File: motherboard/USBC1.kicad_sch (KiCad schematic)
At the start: 24 parts, among them J1 USB_C_Receptacle, U10 TPD4E02B04, U29 TVS2200DRV, U6 SY6280AAC, U7 FUSB302BMPX, U8 TPD4E02B04, U9 TPD4E02B04

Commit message: v0.2 75 routes left!
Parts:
- added R55: 10k, Resistor_SMD:R_0402_1005Metric, symbol Device:R_Small
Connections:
- net +3.3V: now also R55.1
- net FUSB_INT: now also R55.2
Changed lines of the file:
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@@
 	)
 	(junction
+		(at 100.33 109.22)
+		(diameter 0)
+		(color 0 0 0 0)
+	)
+	(junction
 		(at 156.21 77.47)
 		(diameter 0)
@@
 	)
 	(junction
+		(at 80.01 125.73)
+		(diameter 0)
+		(color 0 0 0 0)
+	)
+	(junction
 		(at 176.53 86.36)
 		(diameter 0)
@@
 	(wire
 		(pts
+			(xy 80.01 109.22) (xy 100.33 109.22)
+		)
+		(stroke
+			(width 0)
+			(type default)
+		)
+	)
+	(wire
+		(pts
 			(xy 129.54 165.1) (xy 120.65 165.1)
 		)
@@
 	(wire
 		(pts
+			(xy 80.01 114.3) (xy 80.01 109.22)
+		)
+		(stroke
+			(width 0)
+			(type default)
+		)
+	)
+	(wire
+		(pts
 			(xy 101.6 43.18) (xy 101.6 44.45)
 		)
@@
 	(wire
 		(pts
-			(xy 97.79 125.73) (xy 111.76 125.73)
+			(xy 76.2 125.73) (xy 80.01 125.73)
 		)
 		(stroke
@@
 	(wire
 		(pts
+			(xy 80.01 119.38) (xy 80.01 125.73)
+		)
+		(stroke
+			(width 0)
+			(type default)
+		)
+	)
+	(wire
+		(pts
 			(xy 156.21 93.98) (xy 166.37 93.98)
 		)
@@
 	(wire
 		(pts
-			(xy 100.33 105.41) (xy 100.33 111.76)
+			(xy 100.33 105.41) (xy 100.33 109.22)
 		)
 		(stroke
@@
 	(wire
 		(pts
+			(xy 100.33 109.22) (xy 100.33 111.76)
+		)
+		(stroke
+			(width 0)
+			(type default)
+		)
+	)
+	(wire
+		(pts
 			(xy 144.78 36.83) (xy 168.91 36.83)
 		)
@@
 	(wire
 		(pts
+			(xy 80.01 125.73) (xy 111.76 125.73)
+		)
+		(stroke
+			(width 0)
+			(type default)
+		)
+	)
+	(wire
+		(pts
 			(xy 111.76 109.22) (xy 114.3 109.22)
 		)
@@
 	(hierarchical_label "FUSB_INT"
 		(shape input)
-		(at 97.79 125.73 180)
+		(at 76.2 125.73 180)
 		(fields_autoplaced yes)
 		(effects
@@
 					(unit 1)
 				)
+			)
+		)
+	)
+	(symbol
+		(lib_id "Device:R_Small")
+		(at 80.01 116.84 0)
+		(unit 1)
+		(exclude_from_sim no)
+		(in_bom yes)
+		(on_board yes)
+		(dnp no)
+		(fields_autoplaced yes)
+		(property "Reference" "R55"
+			(at 82.55 115.5699 0)
+			(effects
+				(font
+					(size 1.27 1.27)
+				)
+				(justify left)
+			)
+		)
+		(property "Value" "10k"
+			(at 82.55 118.1099 0)
+			(effects
+				(font
+					(size 1.27 1.27)
+				)
+				(justify left)
+			)
+		)
+		(property "Footprint" "Resistor_SMD:R_0402_1005Metric"
+			(at 80.01 116.84 0)
+			(effects
+				(font
+					(size 1.27 1.27)
+				)
+				(hide yes)
+			)
+		)
+		(property "Datasheet" "~"
+			(at 80.01 116.84 0)
+			(effects
+				(font
+					(size 1.27 1.27)
+				)
+				(hide yes)
+			)
+		)
+		(property "Description" "Resistor, small symbol"
+			(at 80.01 116.84 0)
+			(effects
+				(font
+					(size 1.27 1.27)
+				)
+				(hide yes)
+			)
+		)
+		(pin "2"
+		)
+		(pin "1"
+		)
+		(instances
+			(project "motherboard"
+				(path "/025fe4d1-0305-4b34-be04-f8d9818125a4/5a05a5d5-9903-4299-8afc-3adba5a323ad"
+					(reference "R55")
+					(unit 1)
+				)

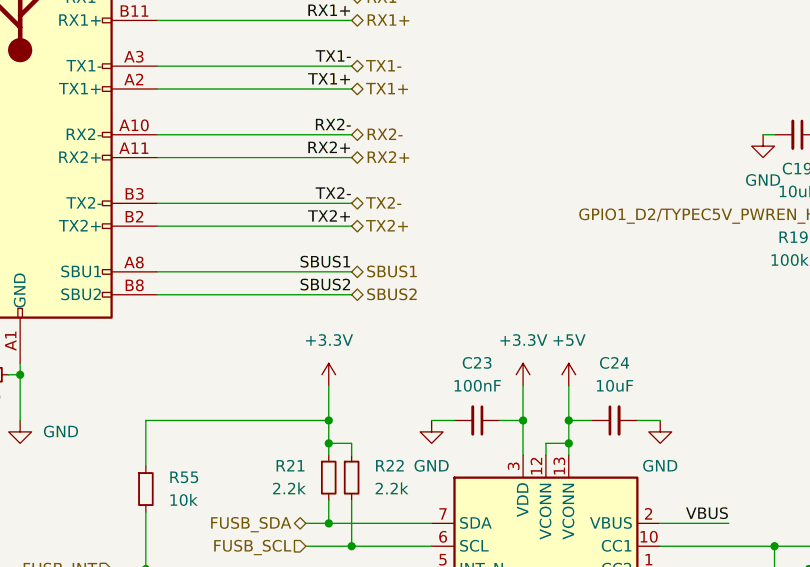
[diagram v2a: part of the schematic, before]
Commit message: v0.2 < 50 unrouted
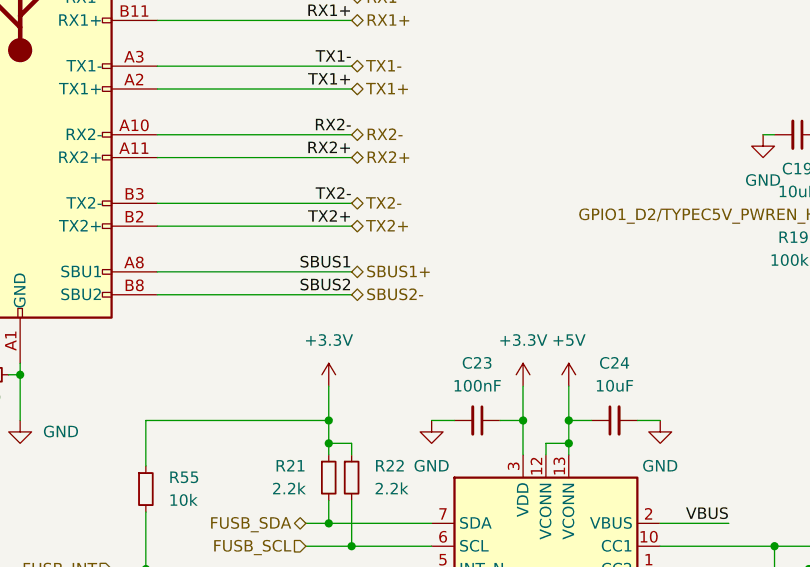
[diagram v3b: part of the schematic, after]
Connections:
- net SBUS1 renamed SBUS1+
- net SBUS2 renamed SBUS2-
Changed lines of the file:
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@@
 		)
 	)
-	(hierarchical_label "SBUS2"
+	(hierarchical_label "SBUS2-"
 		(shape bidirectional)
 		(at 102.87 95.25 0)
@@
 		)
 	)
-	(hierarchical_label "SBUS1"
+	(hierarchical_label "SBUS1+"
 		(shape bidirectional)
 		(at 102.87 92.71 0)

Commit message: mainboard v0.3 + power WIP
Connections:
- net GND: now also U29.1 (GND), U29.2 (GND), U29.3 (GND), U29.7 (GND); no longer U29.4 (IN), U29.5 (IN), U29.6 (IN)
- net VBUS: now also U29.4 (IN), U29.5 (IN), U29.6 (IN); no longer U29.1 (GND), U29.2 (GND), U29.3 (GND), U29.7 (GND)
- net GPIO1_D2/TYPEC5V_PWREN_H renamed GPIO3_B4
- net SBUS1+ renamed SBUS+
- net SBUS2- renamed SBUS-
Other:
- moved on the sheet: U29
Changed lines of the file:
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@@
 	(title_block
 		(title "anyon e")
-		(date "2024-06-12")
-		(rev "V0.1")
+		(date "2024-09-15")
+		(rev "V0.3")
 		(company "Byran Huang")
 		(comment 4 "Proof of concept board for feature verification")
@@
 		)
 	)
-	(label "SBUS2"
+	(label "SBUS-"
 		(at 26.67 154.94 0)
 		(fields_autoplaced yes)
@@
 		)
 	)
-	(label "SBUS1"
+	(label "SBUS+"
 		(at 69.85 170.18 180)
 		(fields_autoplaced yes)
@@
 		)
 	)
-	(label "SBUS2"
+	(label "SBUS-"
 		(at 26.67 160.02 0)
 		(fields_autoplaced yes)
@@
 		)
 	)
-	(label "SBUS2"
+	(label "SBUS-"
 		(at 102.87 95.25 180)
 		(fields_autoplaced yes)
@@
 		)
 	)
-	(label "SBUS1"
+	(label "SBUS+"
 		(at 102.87 92.71 180)
 		(fields_autoplaced yes)
@@
 		)
 	)
-	(label "SBUS1"
+	(label "SBUS+"
 		(at 69.85 165.1 180)
 		(fields_autoplaced yes)
@@
 		)
 	)
-	(hierarchical_label "GPIO1_D2{slash}TYPEC5V_PWREN_H"
+	(hierarchical_label "GPIO3_B4"
 		(shape input)
 		(at 156.21 86.36 180)
@@
 		)
 	)
-	(hierarchical_label "SBUS2-"
+	(hierarchical_label "SBUS-"
 		(shape bidirectional)
 		(at 102.87 95.25 0)
@@
 		)
 	)
-	(hierarchical_label "SBUS1+"
+	(hierarchical_label "SBUS+"
 		(shape bidirectional)
 		(at 102.87 92.71 0)
@@
 	(symbol
 		(lib_id "Power_Protection:TVS2200DRV")
-		(at 168.91 44.45 180)
+		(at 168.91 44.45 0)
+		(mirror y)
 		(unit 1)
 		(exclude_from_sim no)
@@
 		(on_board yes)
 		(dnp no)
-		(fields_autoplaced yes)
 		(property "Reference" "U29"
-			(at 182.88 43.1799 0)
+			(at 182.88 45.7201 0)
 			(effects
 				(font
@@
 		)
 		(property "Value" "TVS2200DRV"
-			(at 182.88 45.7199 0)
+			(at 182.88 43.1801 0)
 			(effects
 				(font
@@
 		)
 		(property "Footprint" "Package_SON:WSON-6-1EP_2x2mm_P0.65mm_EP1x1.6mm"
-			(at 163.83 35.56 0)
+			(at 163.83 53.34 0)
 			(effects
 				(font

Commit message: preparing for motherboard v1.1
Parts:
- renumbered C14 to C33, C15 to C34, C16 to C35, C19 to C36, C20 to C37, C23 to C38, C24 to C39, C25 to C40, C26 to C41, J1 to J10, R18 to R27, R19 to R28, R89 to R29, R90 to R30, R20 to R31, R21 to R32, R22 to R33, R55 to R34, U29 to U11, U6 to U12, U7 to U13, U8 to U14, U9 to U15, U10 to U16
